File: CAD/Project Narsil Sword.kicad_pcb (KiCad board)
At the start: 2 copper layers, 98.6 x 98.9 mm, 7 parts

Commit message: update to files
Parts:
- removed the G*** at (0.00, 0.00) (x7)
- added G*** (x6): LOGO, LOGO, F.Cu at (136.2, 95.4)
- added G***: LOGO, BadgePiratesLogo:shi%%y_B.SLK, B.Cu at (144.7, 68.0)
- added G***: LOGO, BadgePiratesLogo:BadgePiratesURL_B.SLK, F.Cu at (130.2, 100.5)
- added G***: fg, BadgePiratesLogo:FG_B.Cu, F.Cu at (162.9, 68.7)
- added G***: NG_BSilk_B.Cu, BadgePiratesLogo:NG_B.Cu, F.Cu at (173.8, 57.4)
- added G***: BP Logo, BadgePiratesLogo:BPSkull_Distressed_B.SILK, F.Cu at (137.0, 93.9)
- added REF**: Hole_5.5mm(YoMomma), BadgePirates:Hole_5.5mm, F.Cu at (181.5, 49.5)
- added SW1: SW_SPDT, BadgePirates:SW_SPDT_PCM12, B.Cu at (98.6, 142.7)
- added U1: BAT-HLD-006-SMT, BadgePirates:BatteryHolder_LINX_BAT-HLD-012-SMT, B.Cu at (109.3, 120.8)
- added X1: sao_v169bis, BadgePirates:Badgelife-SAOv169-BADGE-2x3_Back, F.Cu at (153.6, 77.3)
- added X2: sao_v169bis, BadgePirates:Badgelife-SAOv169-BADGE-2x3_Back, F.Cu at (132.1, 62.2)
- added X3: sao_v169bis, BadgePirates:Badgelife-SAOv169-BADGE-2x3_Back, F.Cu at (168.2, 98.5)
- added X4: sao_v169bis, BadgePirates:Badgelife-SAOv169-BADGE-2x3_Back, F.Cu at (121.6, 108.8)
- added X5: sao_v169bis, BadgePirates:Badgelife-SAOv169-BADGE-2x3_Back, F.Cu at (91.7, 134.8)
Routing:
- net VCC: track 0.00 -> 178.2 mm
- net +3V3: track 0.00 -> 40.1 mm
- added copper zone on B.Cu, net GND
- added copper zone on F.Cu, net GND
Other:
- board size 98.6 x 98.9 mm -> 99.7 x 100.1 mm
- net class Default removed

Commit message: creating schematic
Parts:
- U1: footprint BadgePirates:BatteryHolder_LINX_BAT-HLD-012-SMT -> BadgePirates:BatteryHolder_MPD_BC2003_1x2032
- moved G*** 15.3 mm to (158.3, 83.3)
- moved X1 11.4 mm to (161.3, 69.0)
- moved X5 4.47 mm to (90.5, 139.1)
- moved X4 3.66 mm to (124.3, 106.4), turned to -45 degrees
- moved U1 1.23 mm to (108.3, 121.5), turned to 45 degrees
- moved 1/0 0.98 mm to (99.5, 143.0)
- renumbered SW1 to 1/0
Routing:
- net VCC: track 178.2 -> 189.2 mm
- net +3V3: track 40.1 -> 42.6 mm

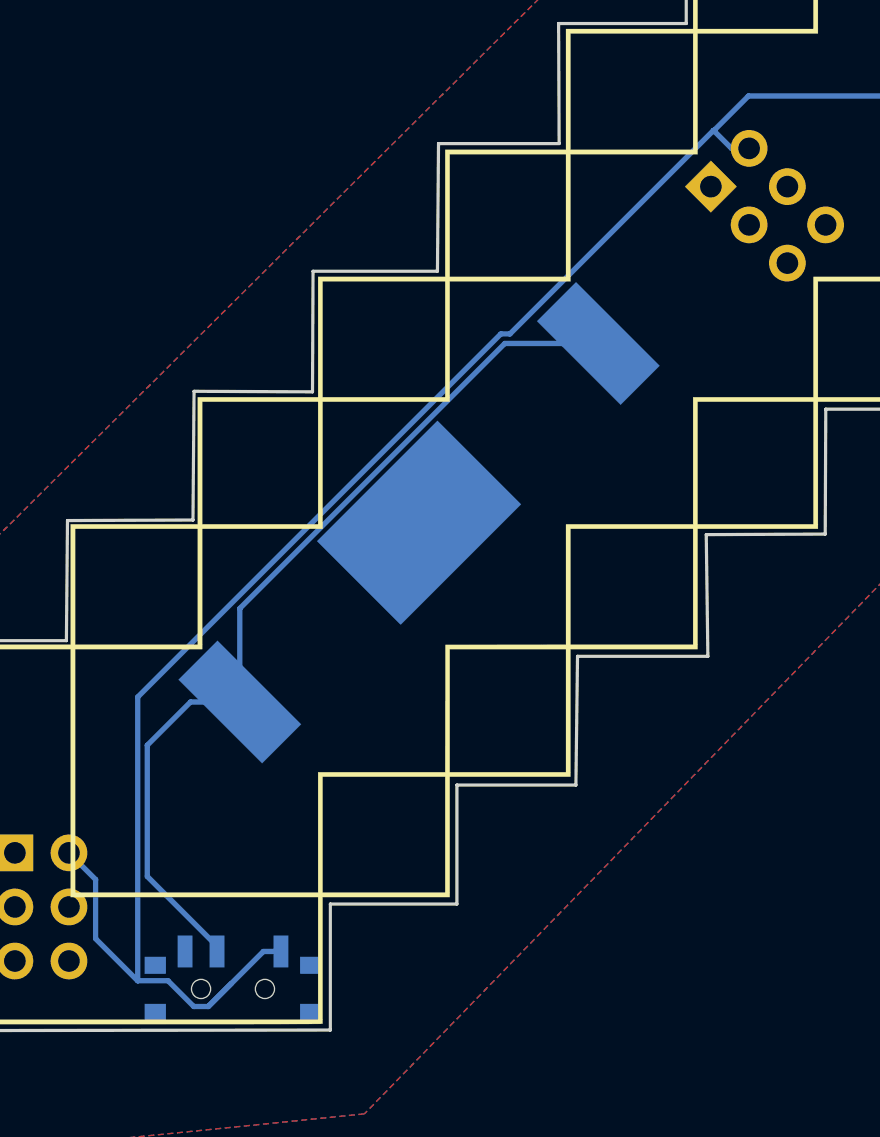
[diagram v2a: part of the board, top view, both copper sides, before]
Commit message: update Battery Footprint
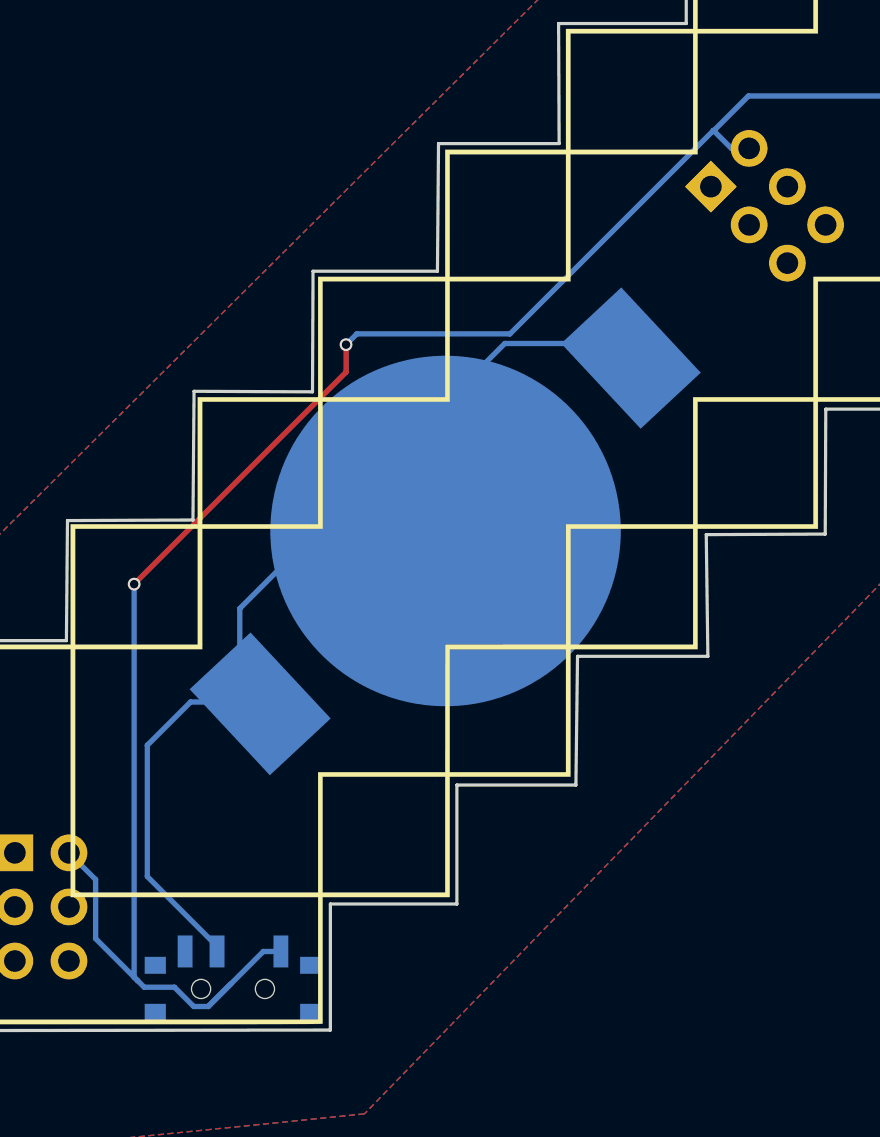
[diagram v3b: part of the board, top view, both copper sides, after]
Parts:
- U1: footprint BadgePirates:BatteryHolder_MPD_BC2003_1x2032 -> BadgePirates:BatteryHolder_MPD_BC2003_1x2032_Fixed
- X1, X2, X3, X4, X5: value sao_v169bis -> sao
- moved U1 1.30 mm to (109.5, 121.8), turned to -137 degrees
- renumbered 1/0 to SW1
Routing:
- net VCC: track 189.2 -> 193.3 mm, vias 0 -> 2

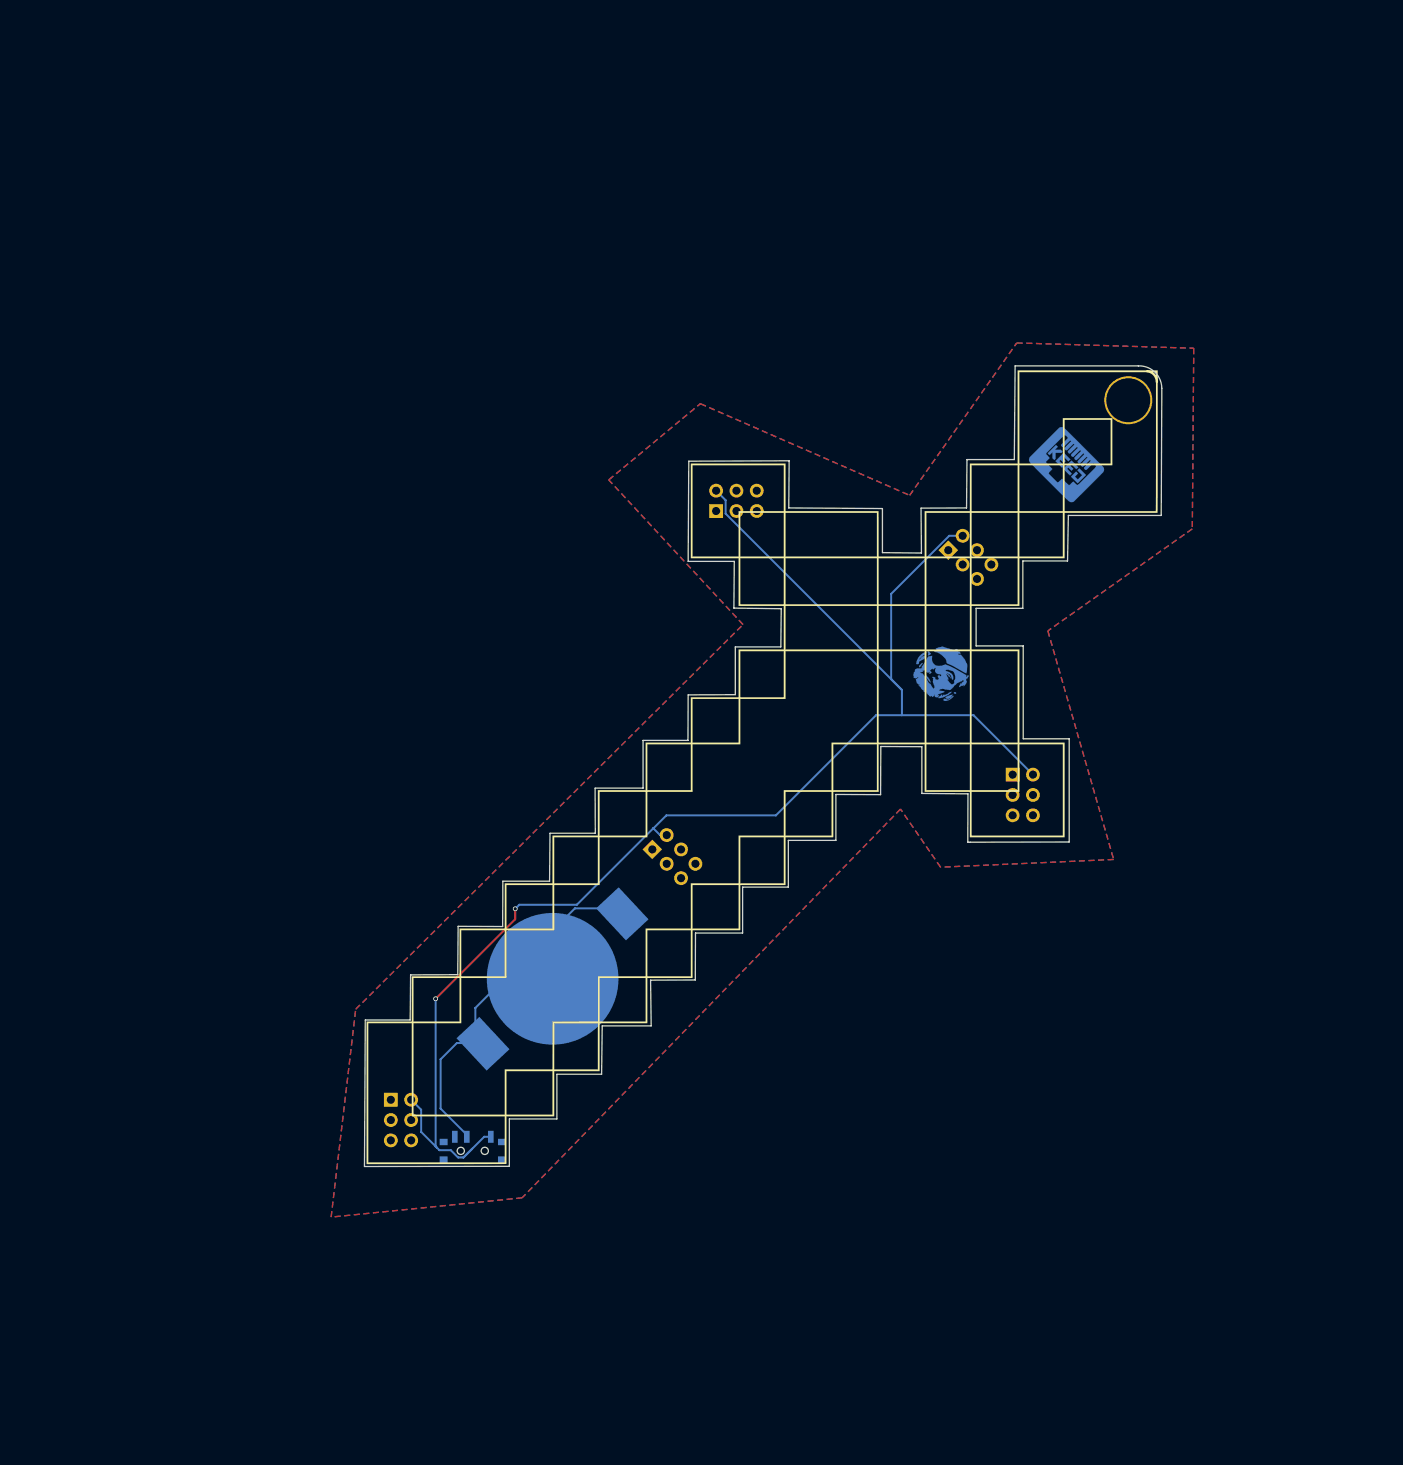
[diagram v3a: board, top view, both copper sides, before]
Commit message: update with fixes, resize and Bigger battery
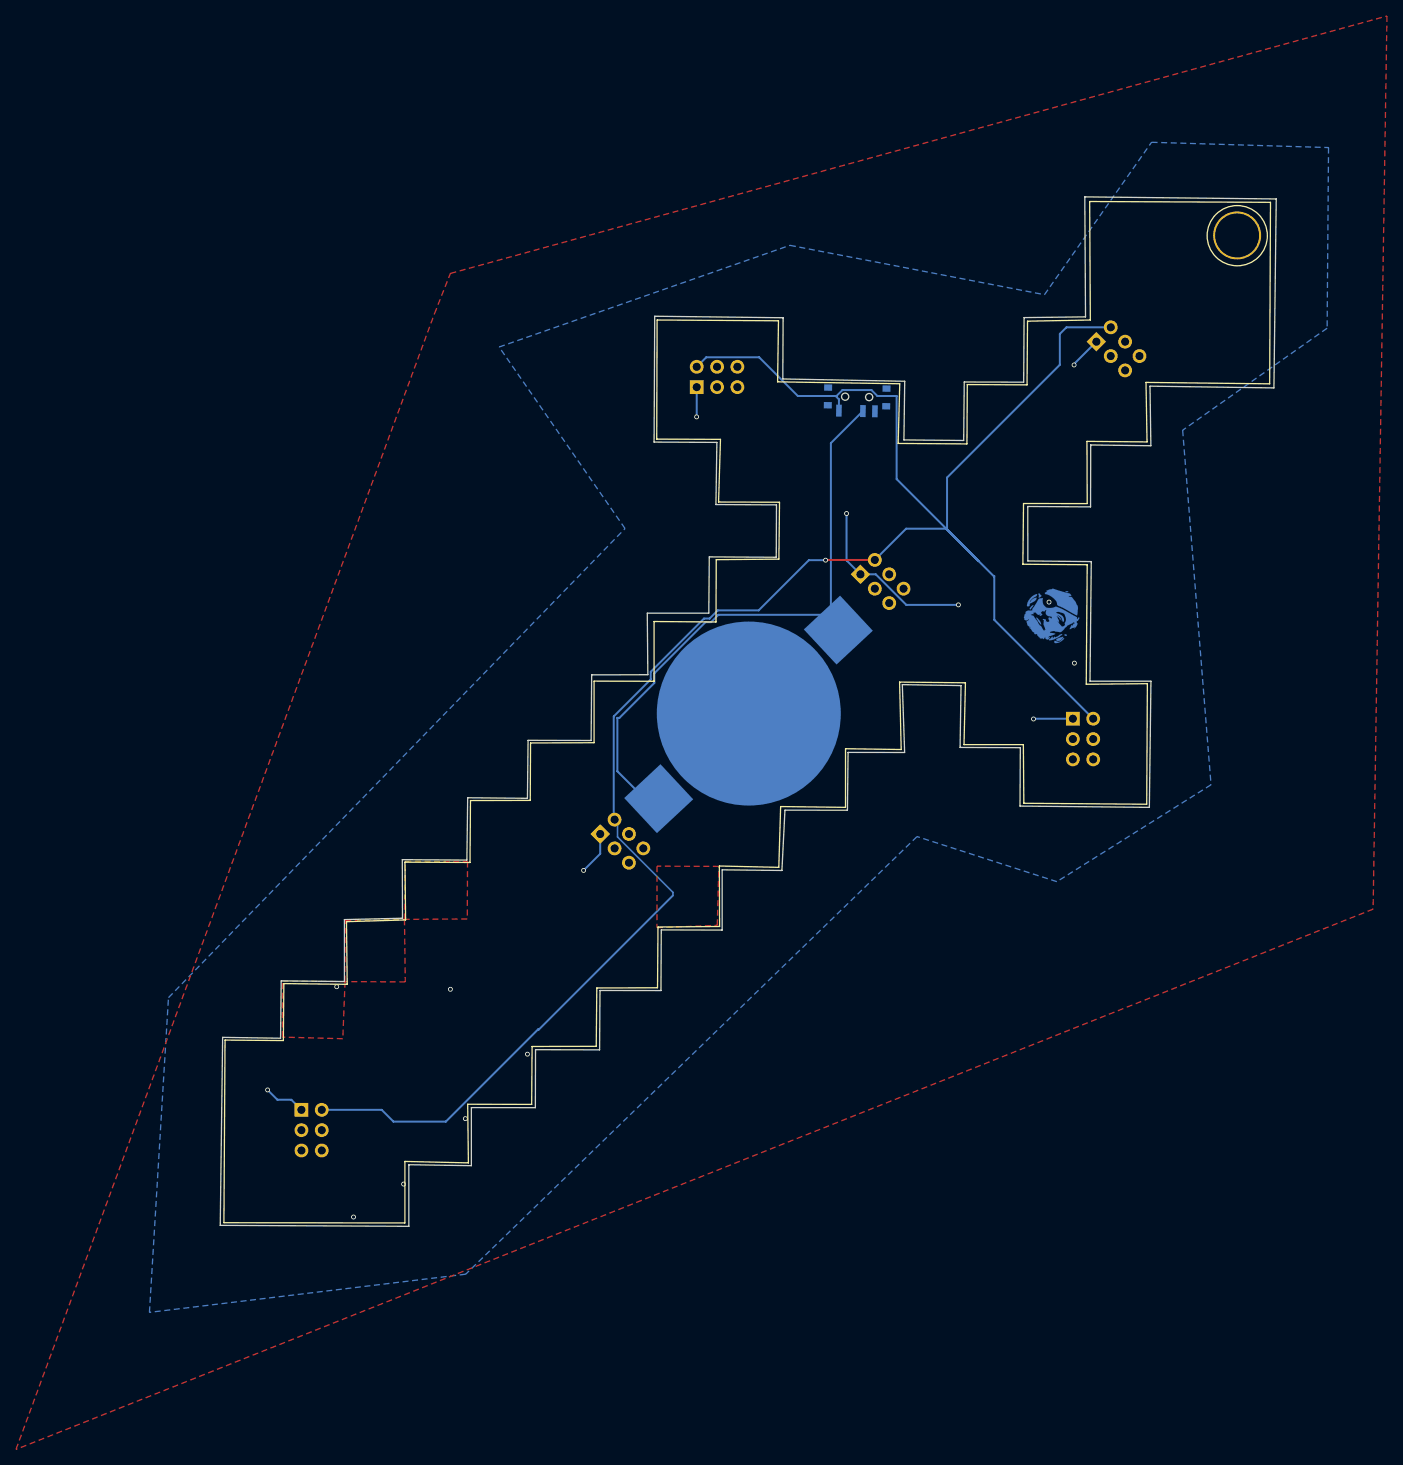
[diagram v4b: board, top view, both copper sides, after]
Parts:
- removed the G*** at (136.2, 95.4) (x2)
- removed the G*** at (173.8, 57.4)
- added G***: LOGO, Project Narsil Sword:F.Mask_g6, F.Cu at (133.3, 91.1)
- added X6: sao, BadgePirates:Badgelife-SAOv169-SAO_Side_B.SLK, F.Cu at (117.8, 104.4)
- U1: value BAT-HLD-006-SMT -> CR2450; footprint BadgePirates:BatteryHolder_MPD_BC2003_1x2032_Fixed -> BadgePirates:BATHLD006SMT - CR2450
- X1, X2, X3, X4, X5: footprint BadgePirates:Badgelife-SAOv169-BADGE-2x3_Back -> BadgePirates:Badgelife-SAOv169-SAO_Side_B.SLK
- moved 1/0 105.2 mm to (147.6, 49.4), turned to -1 degrees
- moved G*** 54.4 mm to (110.9, 110.6)
- moved G*** 50.1 mm to (96.4, 123.2)
- moved X4 43.1 mm to (150.3, 72.0)
- moved U1 41.2 mm to (134.0, 88.7)
- moved G*** 33.4 mm to (101.8, 118.1)
- moved X1 32.0 mm to (179.8, 42.9)
- moved REF** 24.7 mm to (195.1, 28.9)
- moved X2 15.7 mm to (129.7, 46.7)
- moved G*** 15.6 mm to (172.1, 76.1)
- moved X5 11.2 mm to (79.3, 140.4)
- moved X3 10.3 mm to (175.7, 91.5)
- renumbered SW1 to 1/0
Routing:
- net VCC: track 193.3 -> 262.6 mm, vias 2 -> 1
- net GND: track 0.00 -> 54.7 mm, vias 0 -> 15
- net +3V3: track 42.6 -> 79.3 mm
- added copper zone on F.Cu, net (none)
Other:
- board size 99.7 x 100.1 mm -> 132 x 128.7 mm
- board text added: "Rev 1b"
